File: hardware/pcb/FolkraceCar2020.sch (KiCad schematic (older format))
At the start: 0 parts

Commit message: started on schematic design
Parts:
- added J1: Conn_01x02_Male, symbol Connector:Conn_01x02_Male
- added J2: Jetson Nano Header, Connector_PinSocket_2.54mm:PinSocket_2x20_P2.54mm_Vertical, symbol Connector_Generic:Conn_02x20_Odd_Even
- added U1: TPS25940x-Q1, Package_DFN_QFN:QFN-20-1EP_3x4mm_P0.5mm_EP1.65x2.65mm_ThermalVias, symbol DCDC:TPS25940x-Q1
- added U2: OKL-T_6-W12N-C, OKL2T6W12PC, symbol DCDC:OKL-T_6-W12N-C
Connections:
- net labels added: +3V3, +5V, +BATT, AUDIO_MCLK, CAM_AF_EN, GND, GPIO_PE6, GPIO_PZ0, I2C_1_SCL, I2C_1_SDA, I2C_2SDA, I2C_2_SCL, I2S_4_LRCK, I2S_4_SCLK, I2S_4_SDIN, I2S_4_SDOUT, LCD_BL_PWM, LCD_TE, SPI_1_CS0, SPI_1_CS1, SPI_1_MISO, SPI_1_MOSI, SPI_1_SCK, SPI_2_CS0, SPI_2_CS1, SPI_2_MISO, SPI_2_MOSI, SPI_2_SCK, UART_2_CTS, UART_2_RTS, UART_2_RX, UART_2_TX
- wire segments 0 -> 38
- no-connect marks 0 -> 3
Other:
- note added: "Battery Connector"

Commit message: updated schematic
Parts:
- added C1: CP, symbol Device:CP
- added C2, C3, C4: C, symbol Device:C
- added D1: LED RED, LED_SMD:LED_0603_1608Metric, symbol Device:LED
- added D2, D3: LED GREEN, LED_SMD:LED_0603_1608Metric, symbol Device:LED
- added J3: Conn_01x03_Male, Connector_JST:JST_PH_B3B-PH-K_1x03_P2.00mm_Vertical, symbol Connector:Conn_01x03_Male
- added J4: Conn_01x02_Male, Connector_JST:JST_PH_B2B-PH-K_1x02_P2.00mm_Vertical, symbol Connector:Conn_01x02_Male
- added Q1: BSS138, Package_TO_SOT_SMD:SOT-23, symbol Transistor_FET:BSS138
- added Q2: DMN10H220L, Package_TO_SOT_SMD:SOT-23, symbol Transistor_FET:DMN10H220L
- added R1, R10, R11, R12, R2, R3, R4, R6, R7, R8: R, Resistor_SMD:R_0603_1608Metric, symbol Device:R
- added R5: 0, Resistor_SMD:R_0603_1608Metric, symbol Device:R
- added R9: 1.3k, Resistor_SMD:R_0603_1608Metric, symbol Device:R
- added SW1: SPST, Button_Switch_SMD:SW_DIP_SPSTx01_Slide_Omron_A6S-110x_W8.9mm_P2.54mm, symbol Switch:SW_DIP_x01
- added U3: ADS1115IDGS, Package_SO:TSSOP-10_3x3mm_P0.5mm, symbol Analog_ADC:ADS1115IDGS
- U2: footprint OKL2T6W12PC -> DCDC:OKL2T6W12PC
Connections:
- net labels added: FAN_CTRL, IMON, SERVO_PWM, VBUS, VMON
- wire segments 38 -> 146
- no-connect marks 3 -> 5
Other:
- note added: "Fan Control"
- note added: "Negative Logic\nOn/Off"
- note added: "ON/OFF"
- note added: "Power Input eFuse"
- note added: "Servo Connector"
- moved on the sheet: J1, U2

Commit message: added todo in schematic
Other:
- note added: "Todo:\n* Add additional eFuse for motor\n* Add motor controller\n* Add in start module connector & outline for placement\n* Change to horizontal connectors\n* Add connector for hall-sensor\n* Decide on connector for motor\n* Add connector & PMOS for TOF sensor"
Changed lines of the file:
@@
 encoding utf-8
 Sheet 1 1
-Title "Folkrace Car 2020"
+Title "Folkrace Car 2020 laZEr"
 Date "2020-03-18"
 Rev "1.0"
@@
 Wire Wire Line
 	11700 4400 12300 4400
+Text Notes 11800 9950 0    50   ~ 0
+Todo:\n* Add additional eFuse for motor\n* Add motor controller\n* Add in start module connector & outline for placement\n* Change to horizontal connectors\n* Add connector for hall-sensor\n* Decide on connector for motor\n* Add connector & PMOS for TOF sensor
 $EndSCHEMATC

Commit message: added new outline and RP connector
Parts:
- removed J2: Jetson Nano Header, Connector_PinSocket_2.54mm:PinSocket_2x20_P2.54mm_Vertical, symbol Connector_Generic:Conn_02x20_Odd_Even
- added J5: Raspberry_Pi, Connector_PinSocket_2.54mm:PinSocket_2x20_P2.54mm_Vertical, symbol Connector:Raspberry_Pi_2_3
- C4: footprint (none) -> Capacitor_SMD:C_0603_1608Metric
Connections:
- net labels removed: AUDIO_MCLK, CAM_AF_EN, GPIO_PE6, GPIO_PZ0, I2C_1_SCL, I2C_1_SDA, I2C_2SDA, I2C_2_SCL, I2S_4_LRCK, I2S_4_SCLK, I2S_4_SDIN, I2S_4_SDOUT, LCD_BL_PWM, LCD_TE, SPI_1_CS0, SPI_1_CS1, SPI_1_MISO, SPI_1_MOSI, SPI_1_SCK, SPI_2_CS0, SPI_2_CS1, SPI_2_MISO, SPI_2_MOSI, SPI_2_SCK, UART_2_CTS, UART_2_RTS, UART_2_RX, UART_2_TX
- wire segments 146 -> 147
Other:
- moved on the sheet: C4, R11, R12, U3

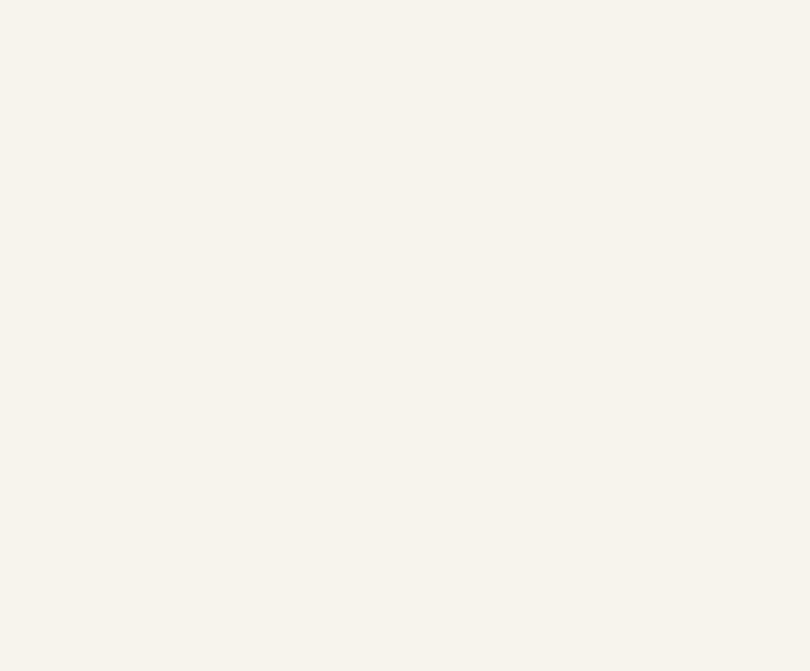
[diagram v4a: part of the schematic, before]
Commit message: added symbol, footprint and 3d model for DRV8874
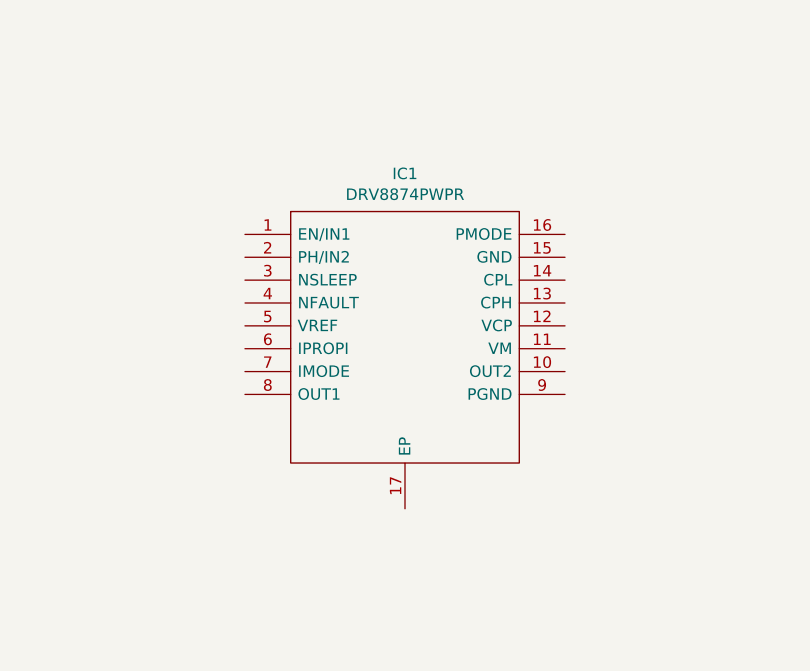
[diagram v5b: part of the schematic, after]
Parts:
- added IC1: DRV8874PWPR, DCDC:SOP65P640X120-17N, symbol DCDC:DRV8874PWPR
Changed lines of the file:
@@
 	10150 5500 10150 5600
 $Comp
-L power:+3V3 #PWR?
+L power:+3V3 #PWR0102
 U 1 1 5E83D1BD
 P 3150 8600
-F 0 "#PWR?" H 3150 8450 50  0001 C CNN
+F 0 "#PWR0102" H 3150 8450 50  0001 C CNN
 F 1 "+3V3" H 3165 8773 50  0000 C CNN
 F 2 "" H 3150 8600 50  0001 C CNN
@@
 	3150 8600 3150 8750
 Connection ~ 3150 8750
+$Comp
+L DCDC:DRV8874PWPR IC1
+U 1 1 5E7B2154
+P 4750 5300
+F 0 "IC1" H 5450 5565 50  0000 C CNN
+F 1 "DRV8874PWPR" H 5450 5474 50  0000 C CNN
+F 2 "DCDC:SOP65P640X120-17N" H 6000 5400 50  0001 L CNN
+F 3 "https://www.ti.com/lit/gpn/DRV8874" H 6000 5300 50  0001 L CNN
+F 4 "H-Bridge Motor Driver With Integrated Current Sense and Regulation" H 6000 5200 50  0001 L CNN "Description"
+F 5 "1.2" H 6000 5100 50  0001 L CNN "Height"
+F 6 "595-DRV8874PWPR" H 6000 5000 50  0001 L CNN "Mouser Part Number"
+F 7 "https://www.mouser.com/Search/Refine.aspx?Keyword=595-DRV8874PWPR" H 6000 4900 50  0001 L CNN "Mouser Price/Stock"
+F 8 "Texas Instruments" H 6000 4800 50  0001 L CNN "Manufacturer_Name"
+F 9 "DRV8874PWPR" H 6000 4700 50  0001 L CNN "Manufacturer_Part_Number"
+	1    4750 5300
+	1    0    0    -1
+$EndComp
 $EndSCHEMATC

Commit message: updated footprint
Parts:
- C3: footprint (none) -> Capacitor_SMD:C_0603_1608Metric
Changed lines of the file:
@@
 F 0 "C3" H 3065 3146 50  0000 L CNN
 F 1 "C" H 3065 3055 50  0000 L CNN
-F 2 "" H 2988 2950 50  0001 C CNN
+F 2 "Capacitor_SMD:C_0603_1608Metric" H 2988 2950 50  0001 C CNN
 F 3 "~" H 2950 3100 50  0001 C CNN
 	1    2950 3100

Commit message: started layout of PCB
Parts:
- added C5: C, symbol Device:C
- added C6: 22nF X7R > 16 V, Capacitor_SMD:C_0402_1005Metric, symbol Device:C_Small
- added C7: C, Capacitor_SMD:C_0603_1608Metric, symbol Device:C
- added C8: 100nF X7R > 16 V, Capacitor_SMD:C_0402_1005Metric, symbol Device:C_Small
- added C9: 100nF X7R > 16 V, Capacitor_SMD:C_0201_0603Metric, symbol Device:C_Small
- added D4: LED RED, LED_SMD:LED_0603_1608Metric, symbol Device:LED
- added H1, H2, H3, H4: MountingHole_Pad, MountingHole:MountingHole_2.7mm_M2.5_Pad_Via, symbol Mechanical:MountingHole_Pad
- added H5, H6, H7, H8: MountingHole, MountingHole:MountingHole_3.2mm_M3_ISO7380, symbol Mechanical:MountingHole
- added J2: Conn_01x02_Male, Connector_Molex:Molex_Mini-Fit_Jr_5569-02A2_2x01_P4.20mm_Horizontal, symbol Connector:Conn_01x02_Male
- added J6: Conn Hall Effect, Connector_JST:JST_PH_S4B-PH-K_1x04_P2.00mm_Horizontal, symbol Connector:Conn_01x04_Male
- added JP1, JP2: Jumper, Resistor_SMD:R_0603_1608Metric, symbol Device:Jumper_NO_Small
- added R13, R14, R15, R16, R17: R, Resistor_SMD:R_0603_1608Metric, symbol Device:R
- added SW2: SW_MEC_5G, symbol Switch:SW_MEC_5G
- J1: footprint (none) -> Connector_Molex:Molex_Mini-Fit_Jr_5569-02A2_2x01_P4.20mm_Horizontal; DPN (none) -> 538-39-30-0020; Distributor (none) -> Mouser; MPN (none) -> 39-30-0020
- J3: value Conn_01x03_Male -> Conn Servo; footprint Connector_JST:JST_PH_B3B-PH-K_1x03_P2.00mm_Vertical -> Connector_JST:JST_PH_S2B-PH-SM4-TB_1x02-1MP_P2.00mm_Horizontal
- J4: value Conn_01x02_Male -> Conn Fan; footprint Connector_JST:JST_PH_B2B-PH-K_1x02_P2.00mm_Vertical -> Connector_JST:JST_PH_S2B-PH-K_1x02_P2.00mm_Horizontal
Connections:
- net +3V3: now also IC1.5 (VREF)
- net +5V: now also J6.4 (Pin_4), JP1.1, R13.1, R15.2
- net GND: now also IC1.15 (GND), IC1.17 (EP), IC1.9 (PGND), C5.2, C7.1, C9.2, J6.1 (Pin_1), R14.1, R16.1, R17.2
- net VBUS: now also C5.1, JP2.2
- net SCL: now reaches U3.10 (SCL)
- net SCL: now also J5.5 (SCL/GPIO3)
- net IMON_M: now reaches U3.6 (AIN2)
- net IMON_M: now also IC1.6 (IPROPI), C7.2, R14.2
- net SDA: now reaches U3.9 (SDA)
- net SDA: now also J5.3 (SDA/GPIO2)
- net PWM_M: now reaches IC1.1 (EN/IN1)
- net PWM_M: now also J5.32 (PWM0/GPIO12)
- net M2: now reaches IC1.10 (OUT2)
- net M2: now also J2.1 (Pin_1)
- net VM: now reaches IC1.11 (VM)
- net VM: now also C8.2, C9.1, JP1.2, JP2.1
- net at IC1.12 (VCP): now also C8.1
- net at IC1.13 (CPH): now also C6.2
- net at IC1.14 (CPL): now also C6.1
- net at IC1.16 (PMODE): now also R17.1
- net DIR_M: now reaches IC1.2 (PH/IN2)
- net DIR_M: now also J5.31 (GCLK2/GPIO6)
- net at IC1.3 (NSLEEP): now also R15.1
- net at IC1.4 (NFAULT): now also D4.1 (K)
- net at IC1.7 (IMODE): now also R16.2
- net M1: now reaches IC1.8 (OUT1)
- net M1: now also J2.2 (Pin_2)
- new net: SW2.1 (A), SW2.2 (A)
- new net: SW2.3 (B), SW2.4 (B)
- new net: D4.2 (A), R13.2
- new net ME_A: J6.3 (Pin_3)
- new net ME_B: J6.2 (Pin_2)
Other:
- note added: "ADD BULK CAP!!!"
- note added: "Deglitch cap"
- note added: "Mechanical"
- note added: "Motor Driver\nPMODE = 0 -> PH/EN Control mode\nnSLEEP = 1 -> Sleep disabled"
- note added: "Todo:\n* Add additional eFuse for motor\n* Add motor controller\n* Add in start module connector & outline for placement\n* Change to horizontal connectors\n* Add connector for hall-sensor (dir and pulse?) \n dont forget pull-up https://www.pololu.com/product/3081/specs\n* Decide on connector for motor\n* Add connector & PMOS for TOF sensor\n* Status LED (RGB) (Neoxpixel)\n* High current driver o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"
- note removed: "Battery Connector"
- note removed: "Todo:\n* Add additional eFuse for motor\n* Add motor controller\n* Add in start module connector & outline for placement\n* Change to horizontal connectors\n* Add connector for hall-sensor\n* Decide on connector for motor\n* Add connector & PMOS for TOF sensor"
- moved on the sheet: C1, C2, C3, D1, D2, D3, IC1, J5, Q1, R1, R10, R2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

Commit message: worked on pcb layout. Some Schematic def. still to be done
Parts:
- removed C1: CP, symbol Device:CP
- removed SW2: SW_MEC_5G, symbol Switch:SW_MEC_5G
- added C12, C13, C6, C7: C, Capacitor_SMD:C_1206_3216Metric, symbol Device:C
- added C4: C, Capacitor_SMD:C_0603_1608Metric, symbol Device:C
- added J7, J8, J9: Conn_01x06_Male, Connector_JST:JST_PH_B6B-PH-K_1x06_P2.00mm_Vertical, symbol Connector:Conn_01x06_Male
- added MODULE1: Startmodule, Connector_PinHeader_2.54mm:PinHeader_1x04_P2.54mm_Vertical, symbol Connector:Conn_01x04_Male
- added MODULE2: OLED 128x32, Connector_PinHeader_2.54mm:PinHeader_1x04_P2.54mm_Vertical, symbol Connector:Conn_01x04_Male
- added R10, R11, R22, R23, R24, R25, R6, R7: R, Resistor_SMD:R_0603_1608Metric, symbol Device:R
- added SW2, SW3: SW_Push, Button_Switch_SMD:SW_SPST_B3U-1000P-B, symbol Switch:SW_Push
- added TP1: TestPoint, TestPoint:TestPoint_Pad_D1.5mm, symbol Connector:TestPoint
- C1: renamed from C2; footprint (none) -> Capacitor_SMD:C_0603_1608Metric
- C8: renamed from C5; footprint (none) -> Capacitor_SMD:C_1206_3216Metric
- J4: renamed from J3; footprint Connector_JST:JST_PH_S2B-PH-SM4-TB_1x02-1MP_P2.00mm_Horizontal -> Connector_JST:JST_PH_B3B-PH-K_1x03_P2.00mm_Vertical
- J6: footprint Connector_JST:JST_PH_S4B-PH-K_1x04_P2.00mm_Horizontal -> Connector_JST:JST_PH_B4B-PH-K_1x04_P2.00mm_Vertical
- renumbered C8 to C10, C9 to C11, C4 to C2, C7 to C5, C6 to C9, D4 to D1, D1 to D2, D2 to D3, D3 to D4, H5 to H1, H6 to H2, H1 to H3, H2 to H4, H7 to H5, H8 to H6, H3 to H7, H4 to H8, J5 to J2, J2 to J3, J4 to J5, R11 to R1, R4 to R12, R15 to R13, R16 to R14, R6 to R15, R7 to R16, R8 to R17, R17 to R18, R5 to R19, R12 to R2, R9 to R20, R10 to R21, R1 to R3, R2 to R4, R3 to R5, R13 to R8, R14 to R9, U3 to U1, U1 to U2, U2 to U3
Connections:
- net +5V: now also C2.1, U1.8 (VDD), C12.1, C13.1, J7.1 (Pin_1), J8.1 (Pin_1), J9.1 (Pin_1), MODULE1.1 (Pin_1), MODULE2.2 (Pin_2), R10.1, R11.1, R23.1, R25.1, R6.1
- net FAN_CTRL: now also R22.1
- net GND: now also U1.1 (ADDR), C12.2, C13.2, C4.1, C6.2, C7.2, J7.2 (Pin_2), J8.2 (Pin_2), J9.2 (Pin_2), MODULE1.2 (Pin_2), MODULE2.1 (Pin_1), R22.2, R24.2, R7.2, SW2.1, SW3.1
- net ME_A: now also R25.2
- net ME_B: now also R23.2
- net SCL: now also J7.5 (Pin_5), J8.5 (Pin_5), J9.5 (Pin_5), MODULE2.3 (Pin_3)
- net SDA: now also J7.6 (Pin_6), J8.6 (Pin_6), J9.6 (Pin_6), MODULE2.4 (Pin_4)
- net SERVO_PWM: now also J2.33 (PWM1/GPIO13), R24.1
- net VBUS: now also C6.1, C7.1
- net at U1.7 (AIN3): now also TP1.1
- net FAN-: now reaches J5.1 (Pin_1), Q2.3 (D)
- removed net +3V3: C2.1, IC1.5 (VREF), J2.1 (3V3), J2.17 (3V3), U1.8 (VDD)
- new net: C4.2, IC1.5 (VREF), R6.2, R7.1
- new net B1: R10.2, SW2.2
- new net B2: R11.2, SW3.2
- new net GPIO_TOF_1: J9.3 (Pin_3)
- new net GPIO_TOF_2: J7.3 (Pin_3)
- new net GPIO_TOF_3: J8.3 (Pin_3)
- new net Kill_Switch: MODULE1.4 (Pin_4)
- new net Start: MODULE1.3 (Pin_3)
- new net ~SHDN_TOF_1: J9.4 (Pin_4)
- new net ~SHDN_TOF_2: J7.4 (Pin_4)
- new net ~SHDN_TOF_3: J8.4 (Pin_4)
- no-connect marks 5 -> 9
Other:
- note added: "Hall effect\nwheel senor"
- note added: "I2C Adress:\nGND -> 1001000\n"
- note added: "Oled I2C Screen 128x32"
- note added: "TOF Sensors"
- moved on the sheet: J4, J5, J6, Q2
